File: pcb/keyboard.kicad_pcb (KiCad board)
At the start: 4 copper layers, 146 x 98.8 mm, 66 parts, among them J1 USB4510-03-1-A, J2 Battery, J3 Tag-Connect TC2030, Q1 2N7002, SW1 PWR, SW2 Reset, U1 SRV05-4, U2 BQ24075, U3 BT840, Y1 ECS-.327-9-34B-TR

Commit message: #2 Add silkscreen names to buttons, leds and version
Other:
- board text added: "CHARGING"
- board text added: "Left-board v1.0"
- board text added: "POWER"
- board text added: "RESET"
- board text added: "STATUS"
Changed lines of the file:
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@@
     (property "ki_keywords" "switch single-pole double-throw spdt ON-ON")
     (attr smd)
-    (fp_text reference "SW1" (at 0 -3.2 90) (layer "F.SilkS")
+    (fp_text reference "SW1" (at 5.175 -0.15 180) (layer "F.SilkS") hide
         (effects (font (size 1 1) (thickness 0.15)))
     )
@@
     (property "ki_keywords" "switch normally-open pushbutton push-button")
     (attr smd)
-    (fp_text reference "SW2" (at 0 -4.5 90) (layer "F.SilkS")
+    (fp_text reference "SW2" (at 0.025 -0.475 90) (layer "F.SilkS") hide
         (effects (font (size 1 1) (thickness 0.15)))
     )
@@
     (property "ki_keywords" "LED diode light-emitting-diode")
     (attr smd)
-    (fp_text reference "LED2" (at -3.3875 0.05) (layer "F.SilkS")
+    (fp_text reference "LED2" (at -3.3875 0.05) (layer "F.SilkS") hide
         (effects (font (size 1 1) (thickness 0.15)))
     )
@@
     (property "ki_keywords" "LED diode light-emitting-diode")
     (attr smd)
-    (fp_text reference "LED1" (at -3.3375 0.05) (layer "F.SilkS")
+    (fp_text reference "LED1" (at -3.3375 0.05) (layer "F.SilkS") hide
         (effects (font (size 1 1) (thickness 0.15)))
     )
@@
   (gr_line (start 167.081779 78.766052) (end 159.279155 86.490645)
     (stroke (width 0.2) (type solid)) (layer "Edge.Cuts"))
+  (gr_text "Left-board v1.0" (at 173.85 149.325) (layer "F.SilkS")
+    (effects (font (size 2 2) (thickness 0.15)) (justify left bottom))
+  )
+  (gr_text "STATUS" (at 268.85 90.425) (layer "F.SilkS")
+    (effects (font (size 1 1) (thickness 0.15)) (justify left bottom))
+  )
+  (gr_text "CHARGING" (at 266.65 88.525) (layer "F.SilkS")
+    (effects (font (size 1 1) (thickness 0.15)) (justify left bottom))
+  )
+  (gr_text "RESET" (at 270.25 129.725 90) (layer "F.SilkS")
+    (effects (font (size 1 1) (thickness 0.15)) (justify left bottom))
+  )
+  (gr_text "POWER" (at 272.125 118.4 90) (layer "F.SilkS")
+    (effects (font (size 1 1) (thickness 0.15)) (justify left bottom))
+  )
   (via (at 270.75 107.55) (size 0.7) (drill 0.3) (layers "F.Cu" "B.Cu") (net 1))
   (via (at 270.5 95) (size 0.7) (drill 0.3) (layers "F.Cu" "B.Cu") (net 1))
@@
   (zone (net 4) (net_name "GND") (layer "In2.Cu") (name "GND") (hatch edge 0.5)
     (connect_pads (clearance 0.508))
-    (min_thickness 0.25) (filled_areas_thickness no)
+    (min_thickness 0.3) (filled_areas_thickness no)
     (fill yes (thermal_gap 0.5) (thermal_bridge_width 0.5))
     (polygon

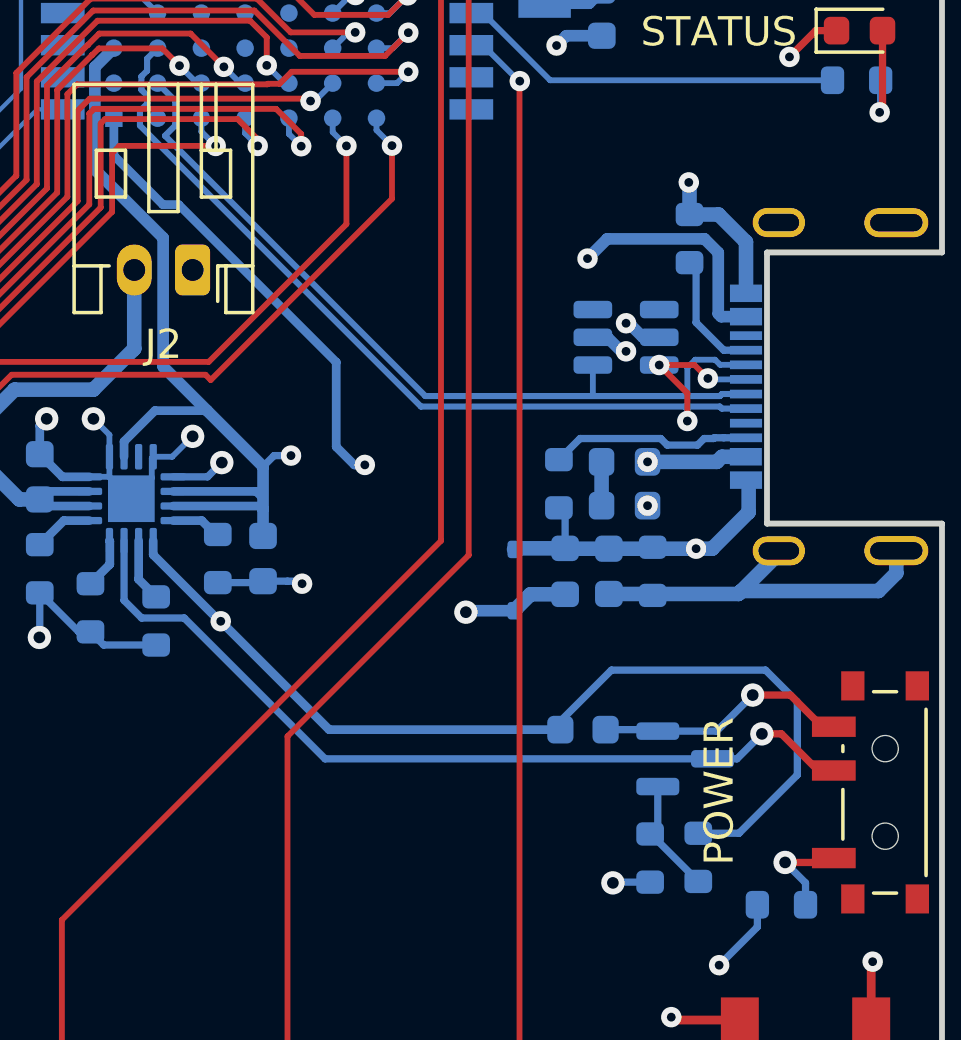
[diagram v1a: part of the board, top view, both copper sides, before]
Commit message: fix: change USB footprint to comply with 0.3mm copper-to-edge constraint
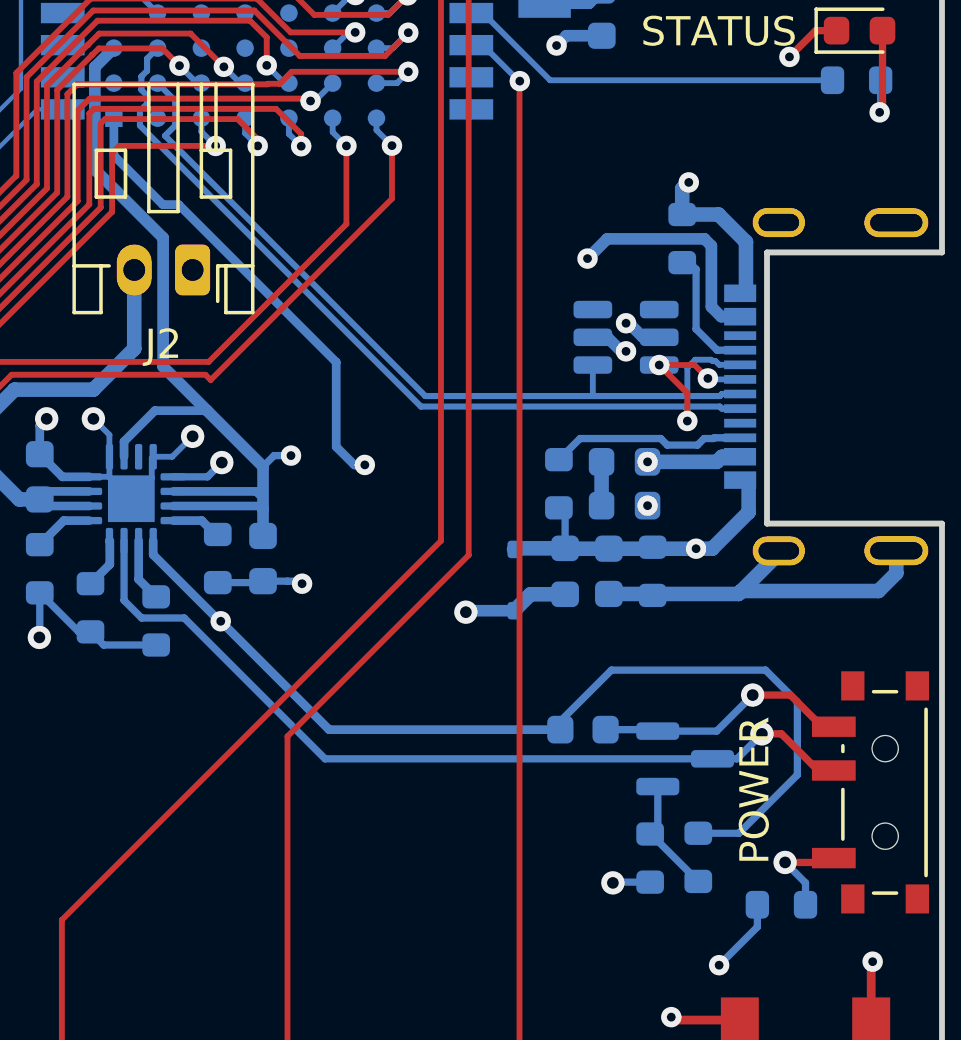
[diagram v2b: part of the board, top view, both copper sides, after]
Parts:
- moved R3 0.25 mm to (270.3, 96.9)
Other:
- rule pad_to_mask_clearance: 0.05 -> 0
